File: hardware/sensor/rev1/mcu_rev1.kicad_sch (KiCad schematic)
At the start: 20 parts, among them IC1 STM8L051F3P6, J1 22-28-4044, J2 M20-9770342

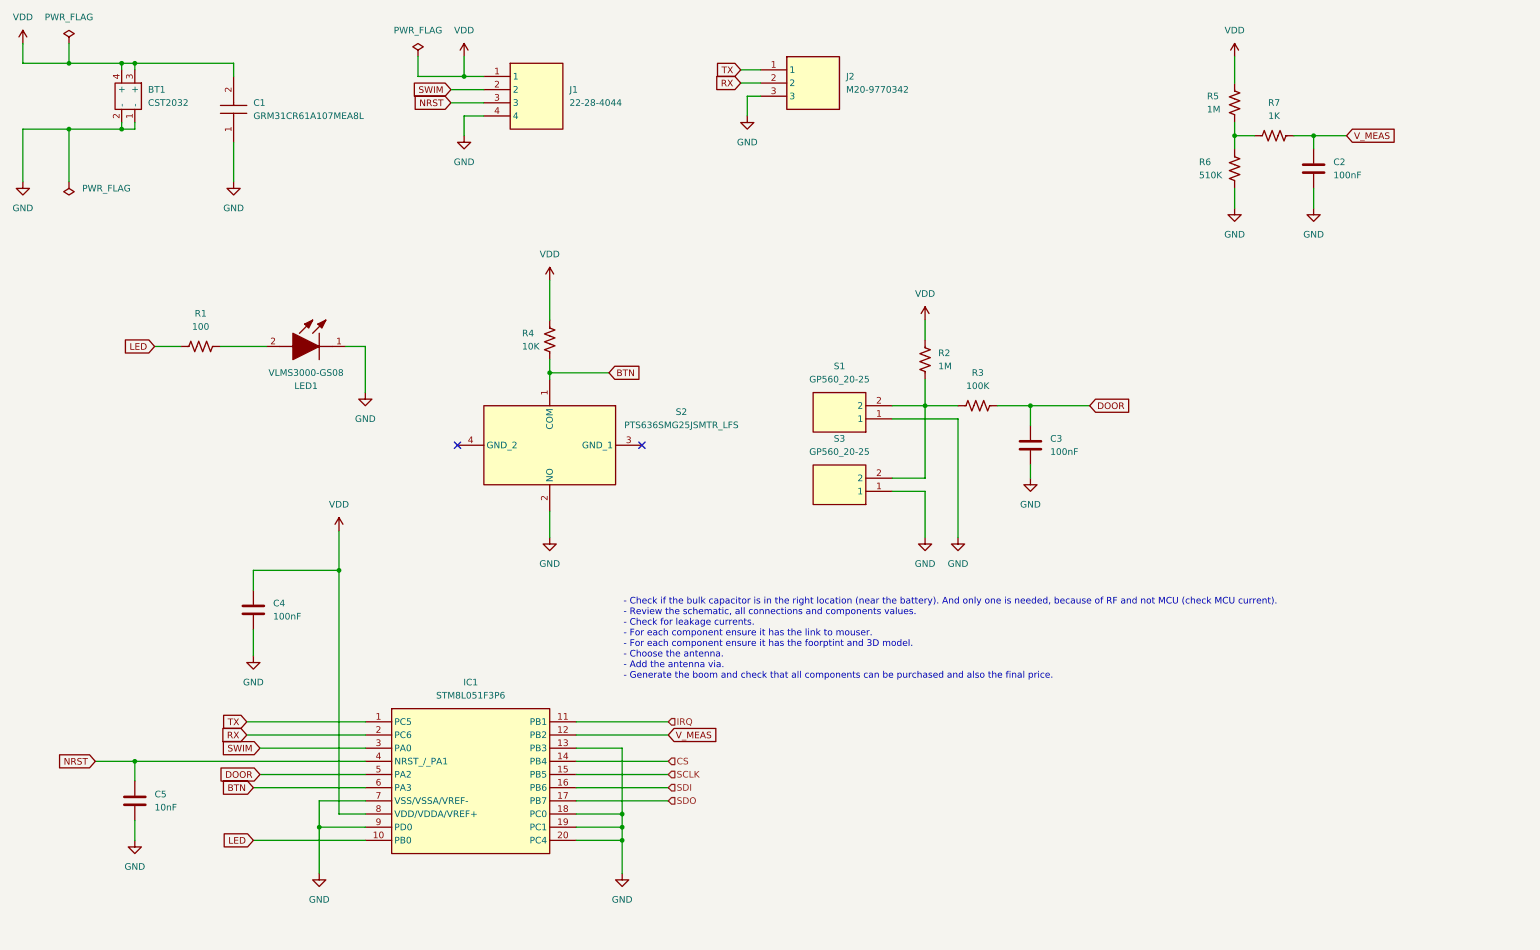
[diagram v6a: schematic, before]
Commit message: EG-49 Adapted the MCU schematic ADC interface, reed interface and button interface. In summary, less components.
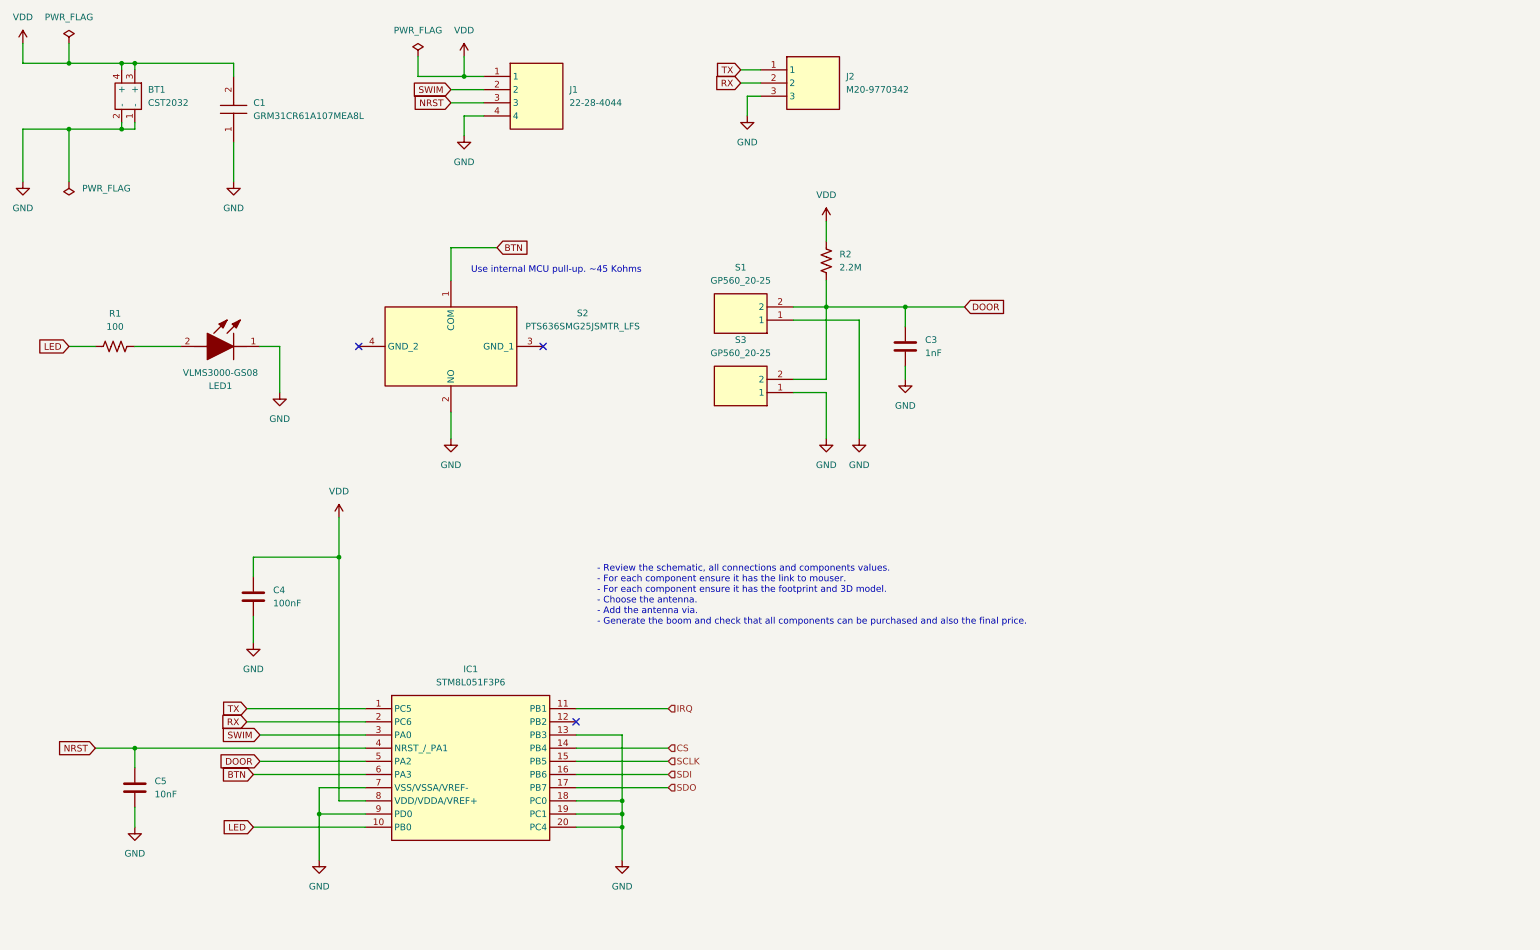
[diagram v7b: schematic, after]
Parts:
- removed C2: 100nF, Capacitor_SMD:C_0603_1608Metric, symbol Device:C
- removed R3: 100K, Resistor_SMD:R_0603_1608Metric, symbol Device:R_US
- removed R4: 10K, Resistor_SMD:R_0603_1608Metric, symbol Device:R_US
- removed R5: 1M, Resistor_SMD:R_0603_1608Metric, symbol Device:R_US
- removed R6: 510K, Resistor_SMD:R_0603_1608Metric, symbol Device:R_US
- removed R7: 1K, Resistor_SMD:R_0603_1608Metric, symbol Device:R_US
- C3: value 100nF -> 1nF; Manufacturer Wurth Elektronik -> KEMET; Manufacturer Part Number 885012206020 -> C0603C102K8RACTU; Mouser Part Number 710-885012206020 -> 80-C0603C102K8R; Supplier Link https://pt.mouser.com/en/ProductDetail/Wurth-Elektronik/885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 -> https://www.mouser.co.uk/en/ProductDetail/KEMET/C0603C102K8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
- R2: value 1M -> 2.2M; Manufacturer Part Number RC0603JR-101ML -> AA0603FR-072M2L; Mouser Part Number 603-RC0603JR-101ML -> 603-AA0603FR-072M2L; Supplier Link https://pt.mouser.com/en/ProductDetail/YAGEO/RC0603JR-101ML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 -> https://pt.mouser.com/en/ProductDetail/YAGEO/AA0603FR-072M2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
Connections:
- net DOOR: now also R2.1, S1.2, S3.2
- net V_MEAS: no longer names the net of IC1.12 (PB2)
- no-connect marks 2 -> 3
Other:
- note added: "- Review the schematic, all connections and components values. - For each component ensure it has the link to mouser. - For each component ensure it has the footprint and 3D model. - Choose the antenna. - Add the antenna via. - Generate the boom and check that all components can be purchased and also the final price."
- note added: "Use internal MCU pull-up. ~45 Kohms"
- note removed: "- Check if the bulk capacitor is in the right location (near the battery). And only one is needed, because of RF and not MCU (check MCU current). - Review the schematic, all connections and components values. - Check for leakage currents. - For each component ensure it has the link to mouser. - For each component ensure it has the foorptint and 3D model. - Choose the antenna. - Add the antenna vi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"
- moved on the sheet: C3, C4, C5, IC1, LED1, R1, R2, S1, S2, S3
